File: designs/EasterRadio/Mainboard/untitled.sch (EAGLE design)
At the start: 51 parts, among them IC1 74HC595D, IC2 74HC595D, IC3 74HC595D, IC4 Analog Digital

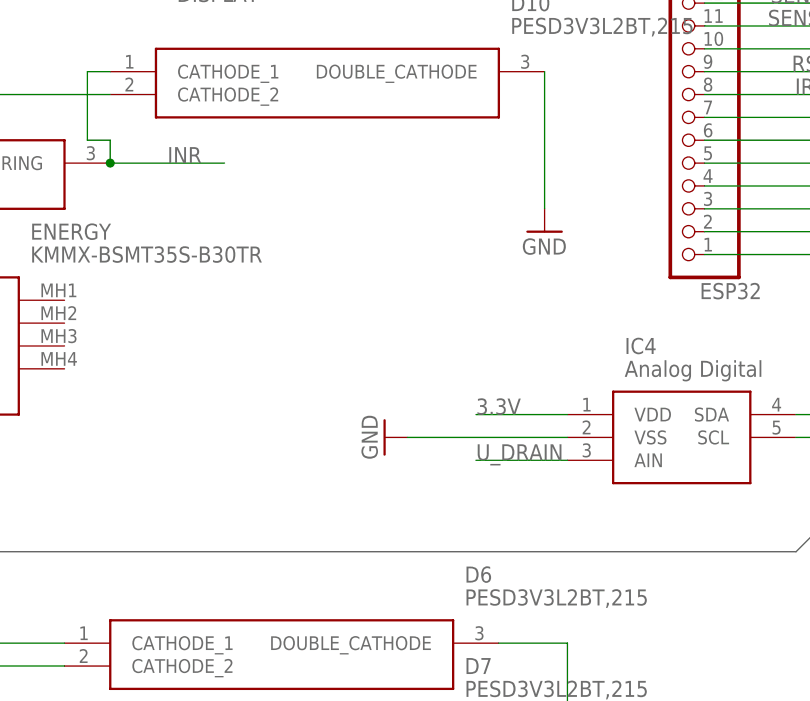
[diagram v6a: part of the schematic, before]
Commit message: changes for new design excluding swap for amplifier
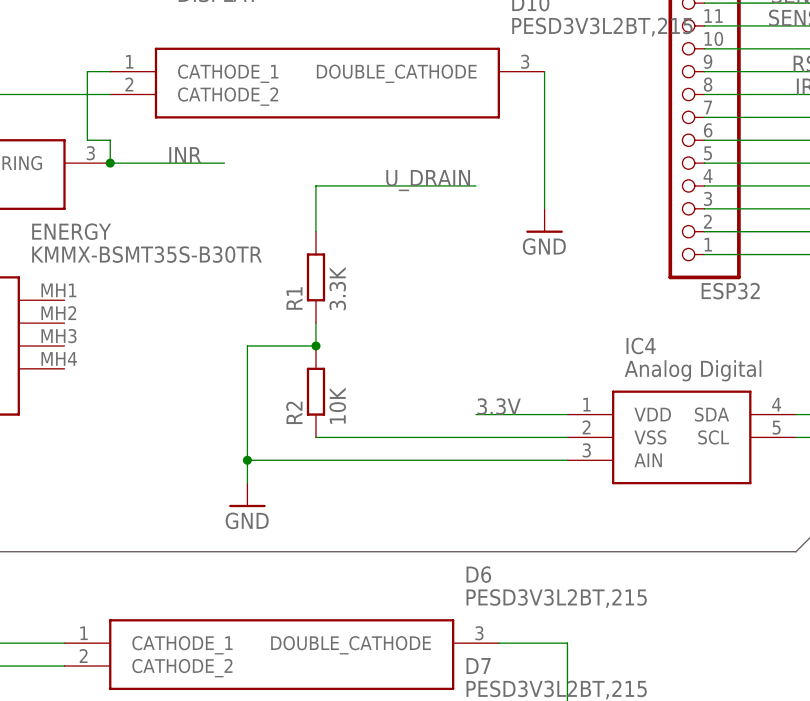
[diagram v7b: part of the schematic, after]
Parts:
- added R1: 3.3K, rcl:R-EU_R0805
- added R2: 10K, rcl:R-EU_R0805
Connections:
- new net N$22: IC4.VSS, R2.1
- net GND: now also IC4.AIN, R1.1, R2.2; no longer IC4.VSS
- net U_DRAIN: now also R1.2; no longer IC4.AIN
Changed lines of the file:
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@@
 <part name="GND1" library="supply1" library_urn="urn:adsk.eagle:library:371" deviceset="GND" device=""/>
 <part name="GND2" library="supply1" library_urn="urn:adsk.eagle:library:371" deviceset="GND" device=""/>
-<part name="GND3" library="supply1" library_urn="urn:adsk.eagle:library:371" deviceset="GND" device=""/>
 <part name="GND5" library="supply1" library_urn="urn:adsk.eagle:library:371" deviceset="GND" device=""/>
 <part name="D4" library="CommonParts" deviceset="LSM115JE3_TR13" device=""/>
@@
 <part name="GND19" library="supply1" library_urn="urn:adsk.eagle:library:371" deviceset="GND" device=""/>
 <part name="D30" library="MouserUseful" deviceset="PESD3V3L2BT,215" device=""/>
+<part name="R1" library="rcl" library_urn="urn:adsk.eagle:library:334" deviceset="R-EU_" device="R0805" package3d_urn="urn:adsk.eagle:package:23553/2" value="3.3K"/>
+<part name="R2" library="rcl" library_urn="urn:adsk.eagle:library:334" deviceset="R-EU_" device="R0805" package3d_urn="urn:adsk.eagle:package:23553/2" value="10K"/>
+<part name="GND3" library="supply1" library_urn="urn:adsk.eagle:library:371" deviceset="GND" device=""/>
 </parts>
 <sheets>
@@
 <attribute name="VALUE" x="203.2" y="195.58" size="1.778" layer="96" rot="R180"/>
 </instance>
-<instance part="GND3" gate="1" x="144.78" y="121.92" smashed="yes" rot="R270">
-<attribute name="VALUE" x="142.24" y="124.46" size="1.778" layer="96" rot="R270"/>
-</instance>
 <instance part="GND5" gate="1" x="248.92" y="256.54" smashed="yes" rot="R180">
 <attribute name="VALUE" x="251.46" y="259.08" size="1.778" layer="96" rot="R180"/>
@@
 <attribute name="NAME" x="341.63" y="101.6" size="1.778" layer="95" align="center-left"/>
 <attribute name="VALUE" x="341.63" y="99.06" size="1.778" layer="96" align="center-left"/>
+</instance>
+<instance part="R1" gate="G$1" x="137.16" y="139.7" smashed="yes" rot="R90">
+<attribute name="NAME" x="135.6614" y="135.89" size="1.778" layer="95" rot="R90"/>
+<attribute name="VALUE" x="140.462" y="135.89" size="1.778" layer="96" rot="R90"/>
+</instance>
+<instance part="R2" gate="G$1" x="137.16" y="127" smashed="yes" rot="R90">
+<attribute name="NAME" x="135.6614" y="123.19" size="1.778" layer="95" rot="R90"/>
+<attribute name="VALUE" x="140.462" y="123.19" size="1.778" layer="96" rot="R90"/>
+</instance>
+<instance part="GND3" gate="1" x="129.54" y="114.3" smashed="yes">
+<attribute name="VALUE" x="127" y="111.76" size="1.778" layer="96"/>
 </instance>
 </instances>
@@
 <wire x1="200.66" y1="175.26" x2="200.66" y2="190.5" width="0.1524" layer="91"/>
 <wire x1="180.34" y1="175.26" x2="200.66" y2="175.26" width="0.1524" layer="91"/>
-</segment>
-<segment>
-<pinref part="IC4" gate="G$1" pin="VSS"/>
-<wire x1="165.1" y1="121.92" x2="147.32" y2="121.92" width="0.1524" layer="91"/>
-<pinref part="GND3" gate="1" pin="GND"/>
 </segment>
 <segment>
@@
 <pinref part="GND19" gate="1" pin="GND"/>
 </segment>
+<segment>
+<pinref part="IC4" gate="G$1" pin="AIN"/>
+<pinref part="R1" gate="G$1" pin="1"/>
+<pinref part="R2" gate="G$1" pin="2"/>
+<wire x1="137.16" y1="134.62" x2="137.16" y2="132.08" width="0.1524" layer="91"/>
+<wire x1="137.16" y1="132.08" x2="129.54" y2="132.08" width="0.1524" layer="91"/>
+<junction x="137.16" y="132.08"/>
+<wire x1="129.54" y1="132.08" x2="129.54" y2="119.38" width="0.1524" layer="91"/>
+<wire x1="129.54" y1="119.38" x2="165.1" y2="119.38" width="0.1524" layer="91"/>
+<wire x1="129.54" y1="119.38" x2="129.54" y2="116.84" width="0.1524" layer="91"/>
+<junction x="129.54" y="119.38"/>
+<pinref part="GND3" gate="1" pin="GND"/>
+</segment>
 </net>
 <net name="RXD0" class="1">
@@
 <net name="U_DRAIN" class="0">
 <segment>
-<pinref part="IC4" gate="G$1" pin="AIN"/>
-<wire x1="165.1" y1="119.38" x2="154.94" y2="119.38" width="0.1524" layer="91"/>
-<label x="154.94" y="119.38" size="1.778" layer="95"/>
-</segment>
-<segment>
 <pinref part="POWER" gate="A" pin="1"/>
 <wire x1="251.46" y1="233.68" x2="251.46" y2="254" width="0.1524" layer="91"/>
 <label x="251.46" y="251.46" size="1.778" layer="95" rot="R90" align="bottom-right"/>
+</segment>
+<segment>
+<pinref part="R1" gate="G$1" pin="2"/>
+<wire x1="137.16" y1="144.78" x2="137.16" y2="149.86" width="0.1524" layer="91"/>
+<label x="144.78" y="149.86" size="1.778" layer="95"/>
+<wire x1="137.16" y1="149.86" x2="154.94" y2="149.86" width="0.1524" layer="91"/>
 </segment>
 </net>
@@
 <wire x1="297.18" y1="93.98" x2="276.86" y2="93.98" width="0.1524" layer="91"/>
 <label x="281.94" y="93.98" size="1.778" layer="95"/>
+</segment>
+</net>
+<net name="N$22" class="0">
+<segment>
+<pinref part="R2" gate="G$1" pin="1"/>
+<pinref part="IC4" gate="G$1" pin="VSS"/>
+<wire x1="137.16" y1="121.92" x2="165.1" y2="121.92" width="0.1524" layer="91"/>
 </segment>
 </net>
@@
 packages will not be understood (or retained) with this version.
 </note>
+<note version="8.4" severity="warning">
+Since Version 8.4, EAGLE supports properties for SPICE simulation.
+Probes in schematics and SPICE mapping objects found in parts and library devices
+will not be understood with this version. Update EAGLE to the latest version
+for full support of SPICE simulation.
+</note>
 <note version="9.0" severity="warning">
